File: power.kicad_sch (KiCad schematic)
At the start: 59 parts, among them U3 AP2112K-3.3, U4 LM317_TO-252, U5 LMR36520FADDA, U6 CJ431, U8 CJ431, U9 LMR36520FADDA

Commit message: schem: add remaining part numbers to BOM
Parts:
- L1, L5: Basic (none) -> X; JLCPCB Part # (none) -> C177245; Manufacturer (none) -> cjiang (Changjiang Microelectronics Tech); Manufacturer Part Number (none) -> FXL0630-330-M
- R15, R31, R44: Basic (none) -> Y; JLCPCB Part # (none) -> C23186; Manufacturer (none) -> Uniroyal Elec; Manufacturer Part Number (none) -> 0603WAF5101T5E
- R28, R36: Basic (none) -> Y; JLCPCB Part # (none) -> C22797; Manufacturer (none) -> Uniroyal Elec; Manufacturer Part Number (none) -> 0603WAF1302T5E
- R29: Basic (none) -> Y; JLCPCB Part # (none) -> C22809; Manufacturer (none) -> Uniroyal Elec; Manufacturer Part Number (none) -> 0603WAF1502T5E
- R30: Basic (none) -> Y; JLCPCB Part # (none) -> C21190; Manufacturer (none) -> Uniroyal Elec; Manufacturer Part Number (none) -> 0603WAF1001T5E
- R32, R45: Basic (none) -> Y; JLCPCB Part # (none) -> C25803; Manufacturer (none) -> Uniroyal Elec; Manufacturer Part Number (none) -> 0603WAF1003T5E
- R33, R34: Basic (none) -> Y; JLCPCB Part # (none) -> C12447; Manufacturer (none) -> Uniroyal Elec; Manufacturer Part Number (none) -> 0603WAF4022T5E
- R35: Basic (none) -> Y; JLCPCB Part # (none) -> C23046; Manufacturer (none) -> Uniroyal Elec; Manufacturer Part Number (none) -> 0603WAF4991T5E
- R38: Basic (none) -> Y; JLCPCB Part # (none) -> C22843; Manufacturer (none) -> Uniroyal Elec; Manufacturer Part Number (none) -> 0603WAF1501T5E
- R40: Basic (none) -> Y; JLCPCB Part # (none) -> C17471; Manufacturer (none) -> Uniroyal Elec; Manufacturer Part Number (none) -> 0805W8F1500T5E
- R41: Basic (none) -> Y; JLCPCB Part # (none) -> C20638; Manufacturer (none) -> Uniroyal Elec; Manufacturer Part Number (none) -> 0805W8F750JT5E
- R42, R46: Basic (none) -> Y; JLCPCB Part # (none) -> C23159; Manufacturer (none) -> Uniroyal Elec; Manufacturer Part Number (none) -> 0603WAF4301T5E
- R43: Basic (none) -> Y; JLCPCB Part # (none) -> C22764; Manufacturer (none) -> Uniroyal Elec; Manufacturer Part Number (none) -> 0603WAF1101T5E
- U3: Basic (none) -> X; JLCPCB Part # (none) -> C51118; Manufacturer (none) -> Diodes Incorporated; Manufacturer Part Number (none) -> AP2112K-3.3TRG1
- U4: Basic (none) -> Y; JLCPCB Part # (none) -> C75510; Manufacturer (none) -> Unisonic Tech (UTC); Manufacturer Part Number (none) -> LM317AG-TN3-R
- U5, U9: Basic (none) -> X; JLCPCB Part # (none) -> C1858395; Manufacturer (none) -> Texas Instruments; Manufacturer Part Number (none) -> LMR36520FADDAR
- U6, U8: Basic (none) -> Y; JLCPCB Part # (none) -> C3113; Manufacturer (none) -> Jiangsu Changjing Electronics Technology Co., Ltd.; Manufacturer Part Number (none) -> CJ431

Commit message: schem/pcb: update MB10S footprint
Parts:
- D3: footprint Pers:SOIC245P670X290-4N -> Package_SO:OnSemi_751EP_SOIC-4_3.9x4.725mm_P2.54mm
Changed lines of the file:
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@@
 			)
 		)
-		(property "Footprint" "Pers:SOIC245P670X290-4N"
+		(property "Footprint" "Package_SO:OnSemi_751EP_SOIC-4_3.9x4.725mm_P2.54mm"
 			(at 49.53 97.79 0)
 			(effects

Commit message: pcb: initial rough pcb placement
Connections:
- net +12/24DC: now also D3.1, TP10.1; no longer D3.2
- net +12/24AC: now also D3.3; no longer D3.4
- net -12/24AC: now also D3.4; no longer D3.3
- net GND: now also D3.2; no longer D3.1
- net at JP4.1 (A), R40.1: no longer TP10.1
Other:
- moved on the sheet: D3, TP10
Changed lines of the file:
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@@
 	)
 	(rectangle
-		(start 177.8 114.3)
-		(end 259.08 156.21)
-		(stroke
-			(width 0)
-			(type dash)
-		)
-		(fill
-			(type none)
-		)
-	)
-	(rectangle
-		(start 91.44 114.3)
-		(end 172.72 156.21)
-		(stroke
-			(width 0)
-			(type dash)
-		)
-		(fill
-			(type none)
-		)
-	)
-	(rectangle
 		(start 135.89 25.4)
 		(end 175.26 62.23)
@@
 	)
 	(junction
+		(at 82.55 78.74)
+		(diameter 0)
+		(color 0 0 0 0)
+	)
+	(junction
 		(at 189.23 91.44)
 		(diameter 0)
@@
 	)
 	(junction
-		(at 78.74 36.83)
-		(diameter 0)
-		(color 0 0 0 0)
-	)
-	(junction
 		(at 195.58 91.44)
 		(diameter 0)
@@
 	(wire
 		(pts
-			(xy 82.55 68.58) (xy 82.55 82.55)
+			(xy 82.55 68.58) (xy 82.55 78.74)
 		)
 		(stroke
@@
 	(wire
 		(pts
-			(xy 74.93 36.83) (xy 78.74 36.83)
+			(xy 74.93 36.83) (xy 92.71 36.83)
 		)
 		(stroke
@@
 	(wire
 		(pts
+			(xy 82.55 78.74) (xy 82.55 82.55)
+		)
+		(stroke
+			(width 0)
+			(type default)
+		)
+	)
+	(wire
+		(pts
 			(xy 109.22 179.07) (xy 109.22 181.61)
 		)
@@
 	(wire
 		(pts
-			(xy 78.74 36.83) (xy 92.71 36.83)
-		)
-		(stroke
-			(width 0)
-			(type default)
-		)
-	)
-	(wire
-		(pts
 			(xy 215.9 140.97) (xy 215.9 142.24)
 		)
@@
 		)
 	)
+	(rule_area
+		(polyline
+			(pts
+				(xy 172.72 114.3) (xy 91.44 114.3) (xy 91.44 156.21) (xy 172.72 156.21)
+			)
+			(stroke
+				(width 0)
+				(type dash)
+			)
+			(fill
+				(type none)
+			)
+		)
+	)
+	(rule_area
+		(polyline
+			(pts
+				(xy 259.08 114.3) (xy 177.8 114.3) (xy 177.8 156.21) (xy 259.08 156.21)
+			)
+			(stroke
+				(width 0)
+				(type dash)
+			)
+			(fill
+				(type none)
+			)
+		)
+	)
+	(netclass_flag ""
+		(length 2.54)
+		(shape round)
+		(at 93.98 114.3 0)
+		(fields_autoplaced yes)
+		(effects
+			(font
+				(size 1.27 1.27)
+			)
+			(justify left bottom)
+		)
+		(property "Netclass" ""
+			(at -116.84 -3.81 0)
+			(effects
+				(font
+					(size 1.27 1.27)
+				)
+			)
+		)
+		(property "Component Class" "3.5V SMPS"
+			(at 94.6785 111.76 0)
+			(effects
+				(font
+					(size 1.27 1.27)
+					(italic yes)
+				)
+				(justify left)
+			)
+		)
+	)
+	(netclass_flag ""
+		(length 2.54)
+		(shape round)
+		(at 180.34 114.3 0)
+		(fields_autoplaced yes)
+		(effects
+			(font
+				(size 1.27 1.27)
+			)
+			(justify left bottom)
+		)
+		(property "Netclass" ""
+			(at -30.48 -3.81 0)
+			(effects
+				(font
+					(size 1.27 1.27)
+				)
+			)
+		)
+		(property "Component Class" "24V SMPS"
+			(at 181.0385 111.76 0)
+			(effects
+				(font
+					(size 1.27 1.27)
+					(italic yes)
+				)
+				(justify left)
+			)
+		)
+	)
 	(symbol
 		(lib_id "power:GND")
@@
 	(symbol
 		(lib_id "Connector:TestPoint")
-		(at 78.74 36.83 0)
+		(at 82.55 78.74 90)
 		(unit 1)
 		(exclude_from_sim no)
@@
 		(dnp no)
 		(property "Reference" "TP10"
-			(at 77.216 31.496 0)
+			(at 77.47 78.74 90)
 			(effects
 				(font
@@
 		)
 		(property "Value" "TestPoint"
-			(at 81.28 34.7979 0)
+			(at 80.5179 76.2 0)
 			(effects
 				(font
@@
 		)
 		(property "Footprint" "TestPoint:TestPoint_Pad_D2.0mm"
-			(at 83.82 36.83 0)
+			(at 82.55 73.66 0)
 			(effects
 				(font
@@
 		)
 		(property "Datasheet" "~"
-			(at 83.82 36.83 0)
+			(at 82.55 73.66 0)
 			(effects
 				(font
@@
 		)
 		(property "Description" "test point"
-			(at 78.74 36.83 0)
+			(at 82.55 78.74 0)
 			(effects
 				(font
@@
 		)
 		(instances
-			(project ""
+			(project "esp32c6-sensor-devboard"
 				(path "/f6edeef8-7fa0-4f55-9ad8-145372f41e3e/4befa429-10a8-402a-b91d-1560a39651d5"
 					(reference "TP10")
@@
 	(symbol
 		(lib_id "Pers:MB10S")
-		(at 49.53 97.79 0)
+		(at 49.53 97.79 180)
 		(unit 1)
 		(exclude_from_sim no)
@@
 		(dnp no)
 		(property "Reference" "D3"
-			(at 57.658 90.932 0)
+			(at 56.642 93.726 0)
 			(effects
 				(font
@@
 		)
 		(property "Value" "MB10S"
-			(at 57.658 93.472 0)
+			(at 56.642 91.186 0)
 			(effects
 				(font

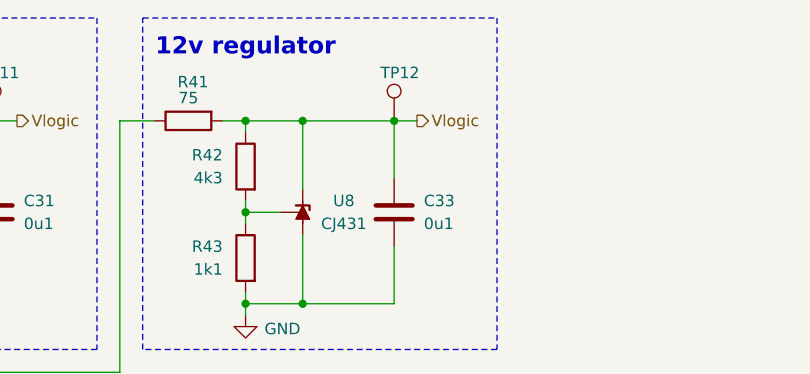
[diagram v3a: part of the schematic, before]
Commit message: pcb: shunt regulators layout
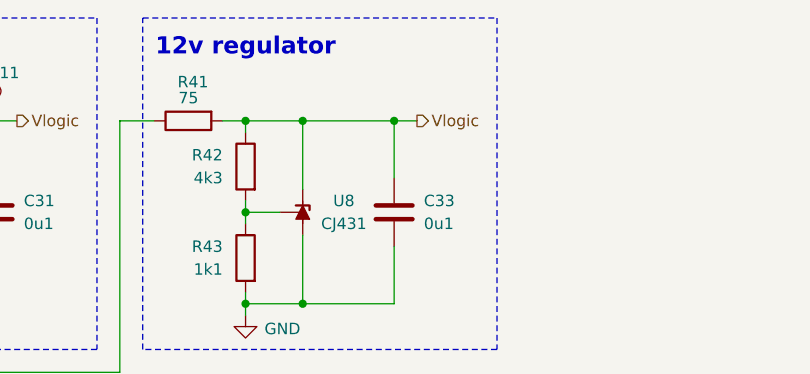
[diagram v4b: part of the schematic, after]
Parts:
- removed TP12: TestPoint, TestPoint:TestPoint_Pad_D2.0mm, symbol Connector:TestPoint
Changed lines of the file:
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@@
-	)
-	(symbol
-		(lib_id "Connector:TestPoint")
-		(at 163.83 36.83 0)
-		(unit 1)
-		(exclude_from_sim no)
-		(in_bom no)
-		(on_board yes)
-		(dnp no)
-		(property "Reference" "TP12"
-			(at 162.306 31.496 0)
-			(effects
-				(font
-					(size 1.27 1.27)
-				)
-				(justify left)
-			)
-		)
-		(property "Value" "TestPoint"
-			(at 166.37 34.7979 0)
-			(effects
-				(font
-					(size 1.27 1.27)
-				)
-				(justify left)
-				(hide yes)
-			)
-		)
-		(property "Footprint" "TestPoint:TestPoint_Pad_D2.0mm"
-			(at 168.91 36.83 0)
-			(effects
-				(font
-					(size 1.27 1.27)
-				)
-				(hide yes)
-			)
-		)
-		(property "Datasheet" "~"
-			(at 168.91 36.83 0)
-			(effects
-				(font
-					(size 1.27 1.27)
-				)
-				(hide yes)
-			)
-		)
-		(property "Description" "test point"
-			(at 163.83 36.83 0)
-			(effects
-				(font
-					(size 1.27 1.27)
-				)
-				(hide yes)
-			)
-		)
-		(pin "1"
-		)
-		(instances
-			(project "esp32c6-sensor-devboard"
-				(path "/f6edeef8-7fa0-4f55-9ad8-145372f41e3e/4befa429-10a8-402a-b91d-1560a39651d5"
-					(reference "TP12")
-					(unit 1)
-				)
-			)
-		)
 	)
 	(symbol
